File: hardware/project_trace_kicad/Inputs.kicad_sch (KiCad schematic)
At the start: 19 parts, among them J101 Conn_Coaxial, J102 Conn_Coaxial, U101 AD8421, U102 AQW280SX, U103 AQW280SX, U201 ADA4807-1

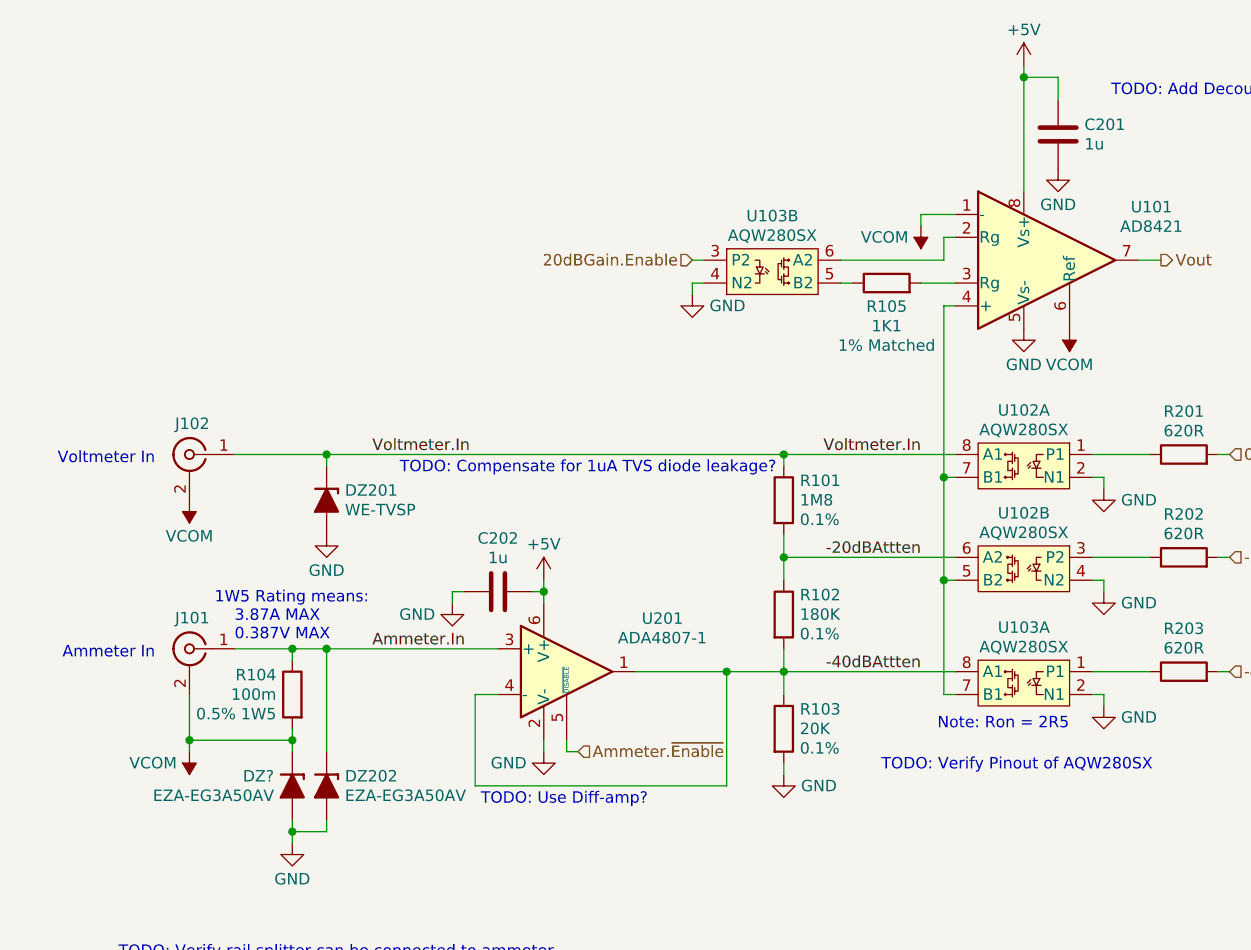
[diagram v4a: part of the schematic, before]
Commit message: Added DAQ_AC and DAC
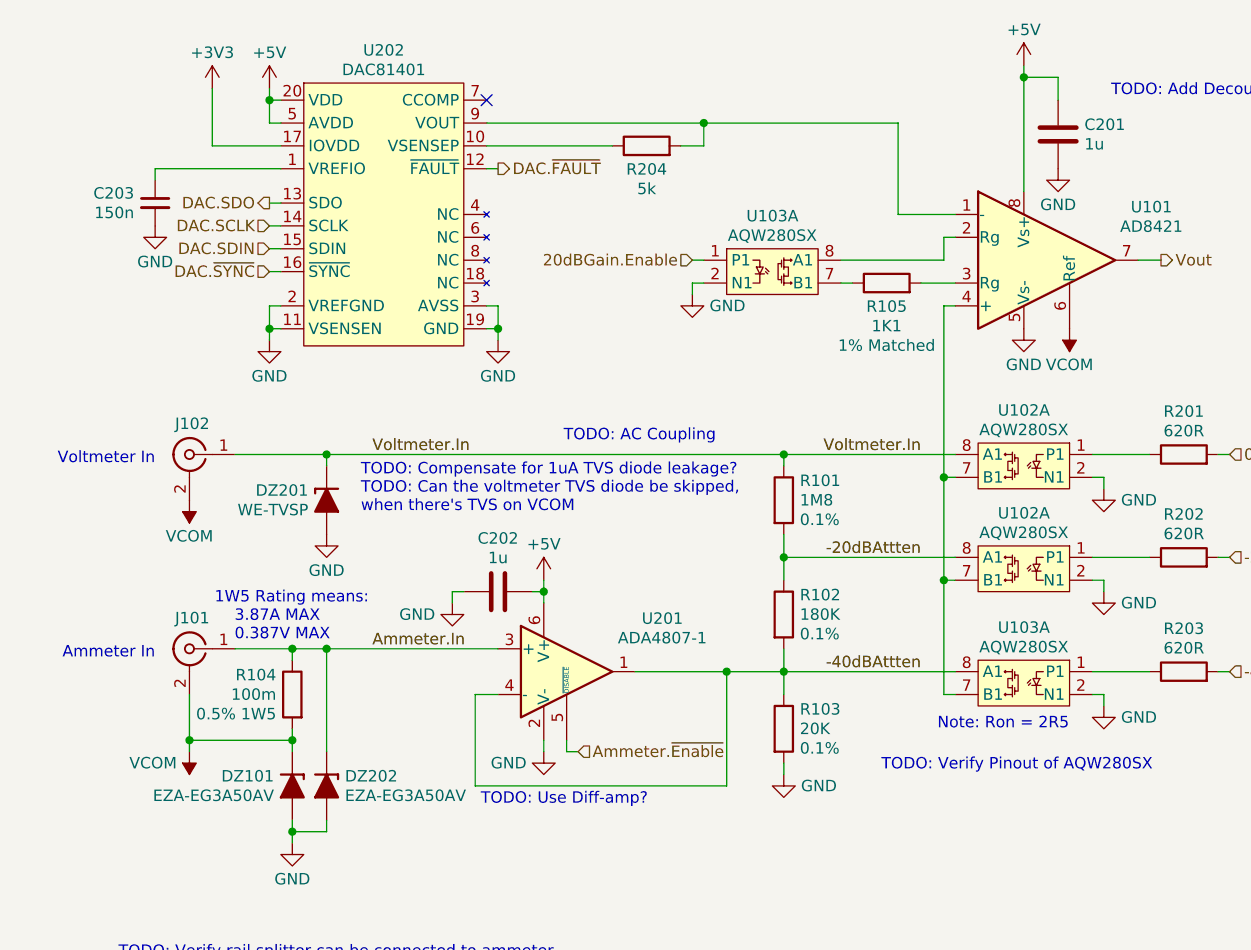
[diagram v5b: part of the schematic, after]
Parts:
- added C203: 150n, symbol Device:C_Small
- added R204: 5k, symbol Device:R
- added U202: DAC81401, Package_SO:Texas_PW0020A_TSSOP-20_4.4x6.5mm_P0.65mm, symbol ProjectTraceSymbols:DAC81401
- gave numbers to parts that had none: 1
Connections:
- net +5V: now also U202.20 (VDD), U202.5 (AVDD)
- net -20dBAttten: now also U102.8 (A1); no longer U102.6 (A2)
- net 20dBGain.Enable: now also U103.1 (P1); no longer U103.3 (P2)
- net GND: now also U102.2 (N1), U103.2 (N1), C203.2, U202.11 (VSENSEN), U202.19 (GND), U202.2 (VREFGND), U202.3 (AVSS); no longer U102.4 (N2), U103.4 (N2)
- net VCOM: no longer U101.1 (-)
- net at R105.1: now also U103.7 (B1); no longer U103.5 (B2)
- net at U101.4 (+), U102.7 (B1), U103.7 (B1): now also U102.7 (B1); no longer U102.5 (B2)
- net at R202.1: now also U102.1 (P1); no longer U102.3 (P2)
- net at U101.2 (Rg): now also U103.8 (A1); no longer U103.6 (A2)
- new net: R204.1, U202.10 (VSENSEP)
- new net: R204.2, U101.1 (-), U202.9 (VOUT)
- new net: C203.1, U202.1 (VREFIO)
- new net +3V3: U202.17 (IOVDD)
- new net DAC.SCLK: U202.14 (SCLK)
- new net DAC.SDIN: U202.15 (SDIN)
- new net DAC.SDO: U202.13 (SDO)
- new net DAC.~{FAULT}: U202.12 (~{FAULT})
- new net DAC.~{SYNC}: U202.16 (~{SYNC})
- no-connect marks 0 -> 1
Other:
- note added: "TODO: AC Coupling"
- note added: "TODO: Can the voltmeter TVS diode be skipped, when there's TVS on VCOM"
- moved on the sheet: DZ201

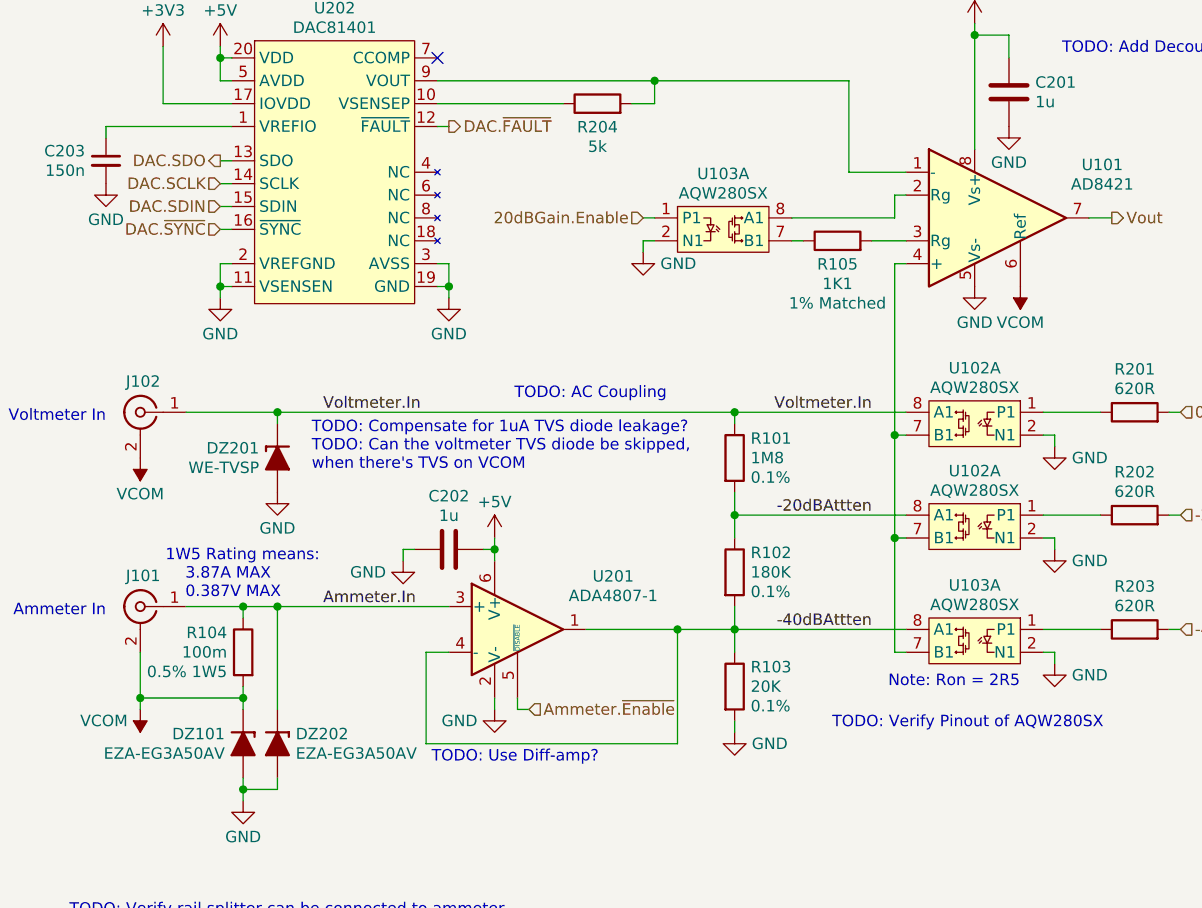
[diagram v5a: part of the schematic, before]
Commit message: Changes to DAQ-AC and Inputs
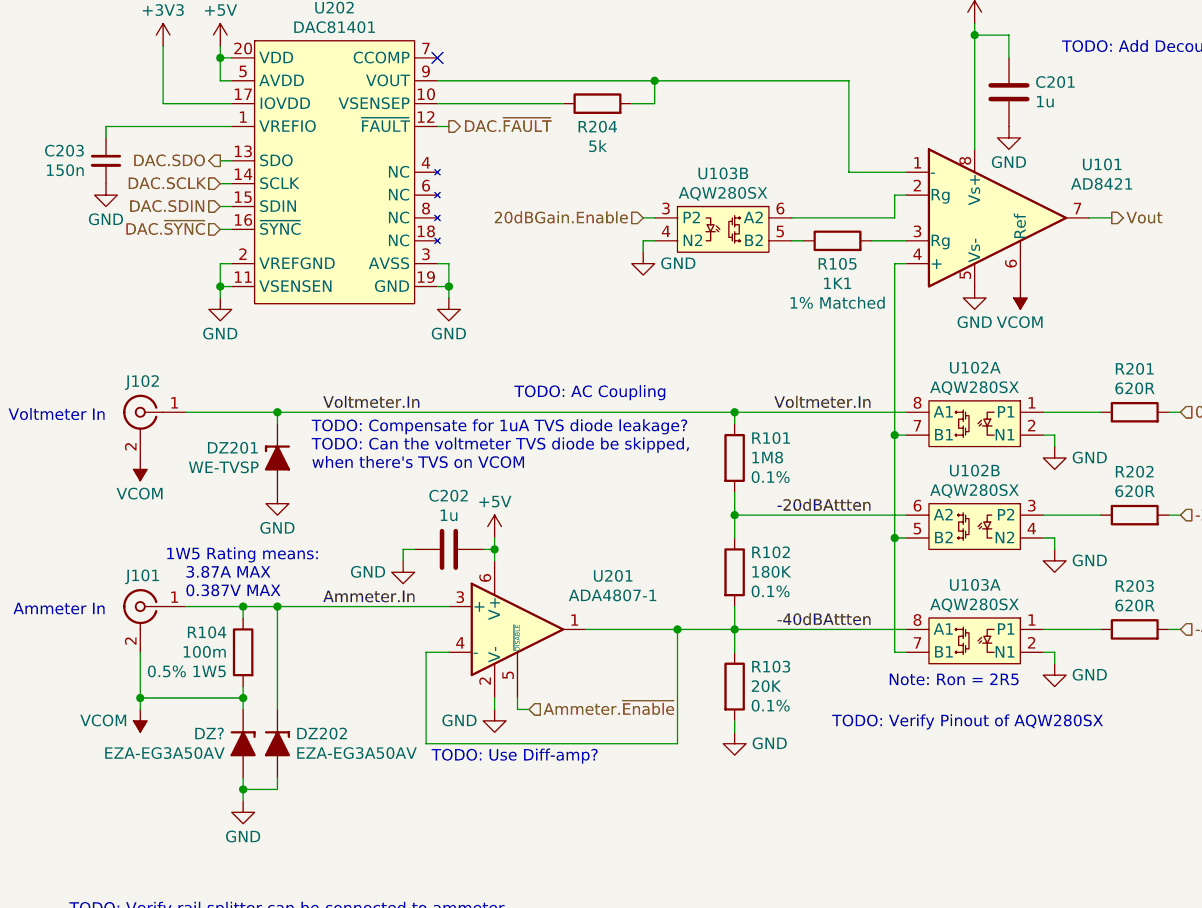
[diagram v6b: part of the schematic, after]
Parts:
- renumbered DZ101 to DZ?
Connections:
- net -20dBAttten: now also U102.6 (A2); no longer U102.8 (A1)
- net 20dBGain.Enable: now also U103.3 (P2); no longer U103.1 (P1)
- net GND: now also U102.4 (N2), U103.4 (N2); no longer U102.2 (N1), U103.2 (N1)
- net at R105.1: now also U103.5 (B2); no longer U103.7 (B1)
- net at U101.4 (+), U102.7 (B1), U103.7 (B1): now also U102.5 (B2); no longer U102.7 (B1)
- net at R202.1: now also U102.3 (P2); no longer U102.1 (P1)
- net at U101.2 (Rg): now also U103.6 (A2); no longer U103.8 (A1)
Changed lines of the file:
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@@
 		(dnp no)
 		(fields_autoplaced yes)
-		(property "Reference" "R?"
+		(property "Reference" "R204"
 			(at 80.01 54.6778 90)
 			(effects
@@
 		(dnp no)
 		(fields_autoplaced yes)
-		(property "Reference" "R?"
+		(property "Reference" "R105"
 			(at 106.68 69.9178 90)
 			(effects
@@
 		(dnp no)
 		(fields_autoplaced yes)
-		(property "Reference" "#PWR?"
+		(property "Reference" "#PWR0105"
 			(at 95.25 128.27 0)
 			(effects
@@
 		(dnp no)
 		(fields_autoplaced yes)
-		(property "Reference" "#PWR0102"
+		(property "Reference" "#PWR?"
 			(at 40.64 135.89 0)
 			(effects
@@
 		(dnp no)
 		(fields_autoplaced yes)
-		(property "Reference" "C?"
+		(property "Reference" "C201"
 			(at 128.651 49.7162 0)
 			(effects
@@
 		(dnp no)
 		(fields_autoplaced yes)
-		(property "Reference" "U?"
+		(property "Reference" "U103"
 			(at 121.92 105.5876 0)
 			(effects
@@
 		(dnp no)
 		(fields_autoplaced yes)
-		(property "Reference" "U?"
+		(property "Reference" "U102"
 			(at 121.92 81.4576 0)
 			(effects
@@
 		(dnp no)
 		(fields_autoplaced yes)
-		(property "Reference" "R?"
+		(property "Reference" "R104"
 			(at 38.862 110.8624 0)
 			(do_not_autoplace yes)
@@
 		(dnp no)
 		(fields_autoplaced yes)
-		(property "Reference" "#PWR?"
+		(property "Reference" "#PWR0111"
 			(at 130.81 96.52 0)
 			(effects
@@
 		(at 121.92 99.06 0)
 		(mirror y)
-		(unit 1)
+		(unit 2)
 		(exclude_from_sim no)
 		(in_bom yes)
@@
 		(dnp no)
 		(fields_autoplaced yes)
-		(property "Reference" "U?"
+		(property "Reference" "U102"
 			(at 121.92 92.8876 0)
 			(effects
@@
 		(dnp no)
 		(fields_autoplaced yes)
-		(property "Reference" "#PWR?"
+		(property "Reference" "#PWR0208"
 			(at 63.5 80.01 0)
 			(effects
@@
 		(dnp no)
 		(fields_autoplaced yes)
-		(property "Reference" "#PWR?"
+		(property "Reference" "#PWR0102"
 			(at 121.92 78.74 0)
 			(effects
@@
 		(dnp no)
 		(fields_autoplaced yes)
-		(property "Reference" "#PWR?"
+		(property "Reference" "#PWR0103"
 			(at 127 68.58 0)
 			(effects
@@
 		(dnp no)
 		(fields_autoplaced yes)
-		(property "Reference" "#PWR?"
+		(property "Reference" "#PWR0211"
 			(at 31.75 49.53 0)
 			(effects
@@
 		(on_board yes)
 		(dnp no)
-		(property "Reference" "C?"
+		(property "Reference" "C203"
 			(at 23.0759 57.3425 0)
 			(effects
@@
 		(dnp no)
 		(fields_autoplaced yes)
-		(property "Reference" "#PWR?"
+		(property "Reference" "#PWR0207"
 			(at 38.1 80.01 0)
 			(effects
@@
 		(dnp no)
 		(fields_autoplaced yes)
-		(property "Reference" "#PWR?"
+		(property "Reference" "#PWR0101"
 			(at 121.92 46.99 0)
 			(effects
@@
 		(dnp no)
 		(fields_autoplaced yes)
-		(property "Reference" "DZ?"
+		(property "Reference" "DZ202"
 			(at 46.482 122.1062 90)
 			(effects
@@
 		(dnp no)
 		(fields_autoplaced yes)
-		(property "Reference" "#PWR?"
+		(property "Reference" "#PWR0206"
 			(at 58.42 109.22 0)
 			(effects
@@
 		(dnp no)
 		(fields_autoplaced yes)
-		(property "Reference" "J?"
+		(property "Reference" "J102"
 			(at 29.5274 82.9416 0)
 			(effects
@@
 		(dnp no)
 		(fields_autoplaced yes)
-		(property "Reference" "C?"
+		(property "Reference" "C202"
 			(at 63.5 95.6816 90)
 			(effects
@@
 		(dnp no)
 		(fields_autoplaced yes)
-		(property "Reference" "U?"
+		(property "Reference" "U202"
 			(at 50.8 41.4526 0)
 			(effects
@@
 		(dnp no)
 		(fields_autoplaced yes)
-		(property "Reference" "#PWR?"
+		(property "Reference" "#PWR0107"
 			(at 130.81 120.65 0)
 			(effects
@@
 		(dnp no)
 		(fields_autoplaced yes)
-		(property "Reference" "#PWR?"
+		(property "Reference" "#PWR0209"
 			(at 38.1 49.53 0)
 			(effects
@@
 		(dnp no)
 		(fields_autoplaced yes)
-		(property "Reference" "#PWR?"
+		(property "Reference" "#PWR0108"
 			(at 85.09 74.93 0)
 			(effects
@@
 		(dnp no)
 		(fields_autoplaced yes)
-		(property "Reference" "DZ?"
+		(property "Reference" "DZ201"
 			(at 42.418 90.3562 90)
 			(effects
@@
 		(dnp no)
 		(fields_autoplaced yes)
-		(property "Reference" "R?"
+		(property "Reference" "R201"
 			(at 139.7 81.5846 90)
 			(effects
@@
 		(dnp no)
 		(fields_autoplaced yes)
-		(property "Reference" "J?"
+		(property "Reference" "J101"
 			(at 29.5274 104.5316 0)
 			(effects
@@
 		(dnp no)
 		(fields_autoplaced yes)
-		(property "Reference" "#PWR?"
+		(property "Reference" "#PWR0104"
 			(at 29.21 115.57 0)
 			(effects
@@
 		(dnp no)
 		(fields_autoplaced yes)
-		(property "Reference" "DZ101"
+		(property "Reference" "DZ?"
 			(at 38.6081 122.1062 90)
 			(effects
@@
 		(dnp no)
 		(fields_autoplaced yes)
-		(property "Reference" "R?"
+		(property "Reference" "R103"
 			(at 97.028 114.6724 0)
 			(effects
@@
 		(dnp no)
 		(fields_autoplaced yes)
-		(property "Reference" "#PWR?"
+		(property "Reference" "#PWR0110"
 			(at 130.81 107.95 0)
 			(effects
@@
 		(dnp no)
 		(fields_autoplaced yes)
-		(property "Reference" "U?"
+		(property "Reference" "U201"
 			(at 81.7587 104.5883 0)
 			(effects
@@
 		(dnp no)
 		(fields_autoplaced yes)
-		(property "Reference" "R?"
+		(property "Reference" "R202"
 			(at 139.7 93.0146 90)
 			(effects
@@
 		(dnp no)
 		(fields_autoplaced yes)
-		(property "Reference" "R?"
+		(property "Reference" "R102"
 			(at 97.028 101.9724 0)
 			(effects
@@
 		(dnp no)
 		(fields_autoplaced yes)
-		(property "Reference" "#PWR?"
+		(property "Reference" "#PWR0201"
 			(at 68.58 125.73 0)
 			(effects
@@
 		(dnp no)
 		(fields_autoplaced yes)
-		(property "Reference" "#PWR?"
+		(property "Reference" "#PWR0210"
 			(at 25.4 67.31 0)
 			(effects
@@
 		(dnp no)
 		(fields_autoplaced yes)
-		(property "Reference" "R?"
+		(property "Reference" "R101"
 			(at 97.028 89.2724 0)
 			(effects
@@
 		(dnp no)
 		(fields_autoplaced yes)
-		(property "Reference" "#PWR?"
+		(property "Reference" "#PWR0205"
 			(at 29.21 87.63 0)
 			(effects
@@
 		(dnp no)
 		(fields_autoplaced yes)
-		(property "Reference" "#PWR?"
+		(property "Reference" "#PWR0202"
 			(at 68.58 104.14 0)
 			(effects
@@
 		(dnp no)
 		(fields_autoplaced yes)
-		(property "Reference" "#PWR?"
+		(property "Reference" "#PWR0203"
 			(at 125.73 60.96 0)
 			(effects
@@
 		(dnp no)
 		(fields_autoplaced yes)
-		(property "Reference" "#PWR?"
+		(property "Reference" "#PWR0204"
 			(at 44.45 101.6 0)
 			(effects
@@
 		(lib_id "ProjectTraceSymbols:AQW280SX")
 		(at 93.98 66.04 0)
-		(unit 1)
+		(unit 2)
 		(exclude_from_sim no)
 		(in_bom yes)
@@
 		(dnp no)
 		(fields_autoplaced yes)
-		(property "Reference" "U?"
+		(property "Reference" "U103"
 			(at 93.98 59.8676 0)
 			(effects
@@
 		(dnp no)
 		(fields_autoplaced yes)
-		(property "Reference" "R?"
+		(property "Reference" "R203"
 			(at 139.7 105.7146 90)
 			(effects
@@
 		(dnp no)
 		(fields_autoplaced yes)
-		(property "Reference" "U?"
+		(property "Reference" "U101"
 			(at 136.0977 58.8683 0)
 			(effects
